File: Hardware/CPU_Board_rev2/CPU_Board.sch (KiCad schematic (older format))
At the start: 103 parts, among them P1 CONN_01X02, P10 CONN_01X02, P11 CONN_01X06, P12 CONN_01X03, P13 CONN_01X01, P14 CONN_01X03, P15 CONN_01X01, P16 CONN_01X01, P17 CONN_01X01, P18 CONN_01X03, P19 CONN_01X01, P2 USB_B, P20 CONN_01X01, P21 CONN_01X01, P22 CONN_01X01, P23 CONN_01X01, P24 CONN_01X01, P3 CONN_01X04, P4 CONN_01X04, P5 CONN_01X06, P6 CONN_01X02, P7 CONN_01X02, P8 CONN_01X02, P9 CONN_01X02, Q1 Q_PMOS_GSD, Q2 Q_PNP_BCE, Q3 Q_PNP_BCE, Q4 N-Channel, Q5 P-Channel, U1 STM32F411RETx, U10 MCDTS2-4N, U11 LPS22HB, U12 INA128, U2 NCP1117DT12G, U3 FT232RL, U4 HTS221, U5 INA128, U6 SPBTLE-RF, U7 A2235-H, U8 LSM303AGR, U9 LSM6DSL, Y1 8MHz

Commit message: PCB Rev 2 on the way
/Somewhat/ done with the layout
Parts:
- removed JP3: Jumper_NC_Small, Pin_Headers:Pin_Header_Straight_2x01_Pitch2.54mm, symbol Jumper_NC_Small
- removed P21, P24: CONN_01X01, Mounting_Holes:MountingHole_2.2mm_M2_DIN965_Pad, symbol CONN_01X01
- removed P6: CONN_01X02, Pin_Headers:Pin_Header_Straight_1x02_Pitch2.54mm, symbol CONN_01X02
- removed Q4: N-Channel, TO_SOT_Packages_SMD:SOT-23_Handsoldering, symbol N-Channel
- removed Q5: P-Channel, TO_SOT_Packages_SMD:SOT-23_Handsoldering, symbol P-Channel
- removed R10, R13: 5360, Resistors_SMD:R_0805_HandSoldering, symbol R
- removed R17, R19, R20: 1k, Resistors_SMD:R_0805_HandSoldering, symbol R
- added P21: CONN_01X06, Custom_Holes:Socket_Strip_Straight_1x06, symbol CONN_01X06
- added P24: CONN_01X06, Connectors_JST:JST_PH_S6B-PH-K_06x2.00mm_Angled, symbol CONN_01X06
- added P25, P26: CONN_01X04, Pin_Headers:Pin_Header_Straight_1x04_Pitch2.54mm, symbol CONN_01X04
- added R10, R13: 5k, Resistors_SMD:R_0805_HandSoldering, symbol R_Small
- added RV1, RV2: 360, Potentiometers:Potentiometer_Trimmer_Bourns_PV36W, symbol POT
- P19, P20, P22, P23: footprint Mounting_Holes:MountingHole_2.2mm_M2_DIN965_Pad -> FOOTPRINTS:MountingHole_2.2mm_M2_DIN965_NoPad
- P3, P4: footprint Pin_Headers:Pin_Header_Straight_1x04_Pitch2.54mm -> Connectors_JST:JST_PH_S4B-PH-K_04x2.00mm_Angled
- U2: footprint TO_SOT_Packages_SMD:TO-263-3Lead -> TO_SOT_Packages_SMD:SOT-223
- Y1: footprint Crystals:Crystal_SMD_EuroQuartz_MQ-4pin_7.0x5.0mm_HandSoldering -> Crystals:Crystal_SMD_HC49-SD
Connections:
- net +3V3: now also P21.6 (P6), P24.6 (P6)
- net +5V: now also C12.1, C16.1, C9.1, L2.2, Q3.2 (C), U2.3 (VI); no longer P1.2 (P2), Q1.3 (D)
- net +5VA: now also P3.4 (P4), P4.4 (P4), U12.7 (V+), U5.7 (V+), P25.4 (P4), P26.4 (P4)
- net BT_5_PA0: no longer P11.6 (P6), R9.2, U6.4 (SPI_IRQ)
- net BT_7_PB3: now also P11.2 (P2); no longer P11.3 (P3)
- net BT_8_PA6: now also P11.3 (P3); no longer P11.2 (P2)
- net GND: now also R16.1, P21.5 (P5), P24.5 (P5)
- net GNDA: now also P3.1 (P1), P4.1 (P1), U12.4 (V-), U12.5 (Ref), U5.4 (V-), U5.5 (Ref), P25.1 (P1), P26.1 (P1)
- net GPS_TOGGLE: now also R16.2, U7.19 (ON_OFF)
- net IMU_I2C_CL: now also P21.2 (P2), P24.2 (P2)
- net IMU_I2C_DA: now also P21.1 (P1), P24.1 (P1)
- net Load_cell_amp_1: now also U12.6; no longer U5.6
- net Load_cell_amp_2: now also U5.6; no longer U12.6
- net VL_C9: now reaches U1.40 (PC9/I2C3_SDA/I2S_CKIN/RCC_MCO_2/SDIO_D1/TIM3_CH4)
- net VL_C9: now also P21.3 (P3), P24.3 (P3)
- net VL_C10: now reaches U1.51 (PC10/I2S3_CK/SDIO_D2/SPI3_SCK)
- net VL_C10: now also P21.4 (P4), P24.4 (P4)
- net at U5.1 (Rg): now also R10.1, RV1.1, RV1.2
- net at P3.2 (P2), U5.2 (-): now also P25.2 (P2)
- net at P3.3 (P3), U5.3 (+): now also P25.3 (P3)
- net at U5.8 (Rg): now also R10.2, RV1.3
- net at U12.1 (Rg): now also R13.1, RV2.3
- net at P4.2 (P2), U12.2 (-): now also P26.2 (P2)
- net at P4.3 (P3), U12.3 (+): now also P26.3 (P3)
- net at U12.8 (Rg): now also R13.2, RV2.1, RV2.2
- new net: P1.2 (P2), Q1.3 (D)
- new net BT_4_PA0: P11.6 (P6), R9.2, U6.4 (SPI_IRQ)
- no-connect marks 58 -> 54
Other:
- note added: "Aimed for: 5.36 kohm"
- note added: "Amplifier for load cell,\nconnects to JST-TH and Analog"
- note added: "Shutdown"
- note added: "Time-of-Flight\nVL530x"
- note removed: "3V3/2 =\n1.65V"
- note removed: "Amplifier for load cell,\nconnects to TH and Analog"
- note removed: "High-speed digital \nswitching logic"
- note removed: "Pull to\nReference"
- moved on the sheet: C14, C18, L2, L3, R16

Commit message: Chackpoint PCB rev2
* Added datasheets for LSM9DS1 and STEVAL board
* Drawn footprints for:
o Connectors (JST)
o LGA-12_2x2mm "Handsolder friendlier"
o LGA-24L_3x3.5 "Handsolder friendlier"
* Drawn symbol for LSM9DS1
* Fixed GPS A2235-H footprints (normal & Handsolder)
* Almost completed MCU-board rev2 schematic (Miss connections for
LSM9DS1)
* Almost completed MCU-board rev2 PCB layout (Miss the connections for
LSM and have only designed internal module layout for all IMU/IMU-like
components.)

Next steps:
* Make space for gigantig STEVAL LSM9DS1 DIP24
* Draw connections to MCU
* Cake
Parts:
- removed C30: 4.7u, Capacitors_SMD:CP_Elec_4x5.3, symbol C
- added C30: 4.7u, Capacitors_SMD:CP_Elec_3x5.3, symbol CP
- added C34, C36, C37, C39: 100n, Capacitors_SMD:C_0805_HandSoldering, symbol C
- added C35: 10uF, Capacitors_SMD:CP_Elec_5x5.3, symbol CP1_Small
- added C38: 10n, Capacitors_SMD:C_0805_HandSoldering, symbol C
- added IM1: LSM9DS1, FOOTPRINTS:LGA-24L_3x3.5mm_Pitch0.43mm_Handsolder, symbol LSM9DS1
- added JP3, JP4: Jumper_NC_Dual, Pin_Headers:Pin_Header_Straight_1x03_Pitch2.54mm, symbol Jumper_NC_Dual
- added JP5: Jumper_NC_Small, Pin_Headers:Pin_Header_Straight_1x02_Pitch2.54mm, symbol Jumper_NC_Small
- added P6: CONN_02X12, Housings_DIP:DIP-24_W10.16mm, symbol CONN_02X12
- added R14: 220, Resistors_SMD:R_0805_HandSoldering, symbol R_Small
- added R17, R19: 10k, Resistors_SMD:R_0805_HandSoldering, symbol R
- C10, C4, C5: footprint Capacitors_SMD:CP_Elec_4x5.3 -> Capacitors_SMD:CP_Elec_3x5.3
- P24: footprint Connectors_JST:JST_PH_S6B-PH-K_06x2.00mm_Angled -> FOOTPRINTS:JST_PH_S6B-PH-K_06x2.50mm_Angled
- P3, P4: footprint Connectors_JST:JST_PH_S4B-PH-K_04x2.00mm_Angled -> FOOTPRINTS:Connector_JST_S4B-ZR_1x4
- U8: footprint Housings_LGA:LGA-12_2x2mm_Pitch0.5mm -> FOOTPRINTS:LGA-12_2x2mm_Pitch0.5mm_Handsolder
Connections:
- net +3V3: now also JP4.2, JP5.1, R17.1, R19.1; no longer D2.1 (K), U2.2 (VO), U2.4 (VO)
- net +5V: now also JP3.2, R14.1; no longer Q3.2 (C)
- net GND: now also C30.2, C34.2, C35.2, C36.2, C37.2, C38.2, C39.2, IM1.14 (RES), IM1.15 (RES), IM1.16 (RES), IM1.17 (RES), IM1.18 (RES), IM1.19 (GND), IM1.20 (GND), P6.13 (P13)
- net IMU_I2C_CL: now also IM1.2 (SCL/SPI), P6.20 (P20), R17.2
- net IMU_I2C_DA: now also R19.2
- net LPS_VDD: now also C30.1
- net USB3V3: now reaches U3.17 (3V3OUT)
- net USB3V3: now also C34.1, JP4.3
- net USB5V: now reaches C6.1, C7.1, C8.1, L1.2, U3.20 (VCC)
- net USB5V: now also JP3.3
- net BT_10_PA1 renamed BT_CL
- net BT_11_PA8 renamed BT_RST
- net BT_4_PA0 renamed BT_IRQ
- net BT_7_PB3 renamed BT_CS
- net BT_8_PA6 renamed BT_MISO
- net BT_9_PA7 renamed BT_MOSI
- new net: JP3.1, Q3.2 (C)
- new net: D2.1 (K), R14.2
- new net: JP4.1, U2.2 (VO), U2.4 (VO)
- new net: C38.1, IM1.21 (CAP)
- new net: C39.1, IM1.24 (C1)
- new net LSM9_CS_A/G: IM1.7 (CS_A/G), P6.19 (P19)
- new net LSM9_CS_M: IM1.8 (CS_M), P6.18 (P18)
- new net LSM9_DEN_A/G: IM1.13 (DEN_A/G), P6.23 (P23)
- new net LSM9_DRDY_M: IM1.9 (DRDY_M), P6.16 (P16)
- new net LSM9_INT1_A/G: IM1.11 (INT_A/G), P6.14 (P14)
- new net LSM9_INT2_A/G: IM1.12 (INT2_A/G), P6.15 (P15)
- new net LSM9_INT_M: IM1.10 (INT_M), P6.17 (P17)
- new net LSM9_SDA: IM1.4 (SDA/SDI/SDO), P6.21 (P21)
- new net LSM9_SDO: IM1.5 (SDO_A/G), IM1.6 (SDO_M), P6.22 (P22)
- new net LSM9_VDD: C35.1, C36.1, C37.1, IM1.1 (VDDIO), IM1.22 (VDD), IM1.23 (VDD), IM1.3 (VDDIO), JP5.2, P6.1 (P1), P6.2 (P2)
- no-connect marks 54 -> 64
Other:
- note added: "IMU Accelerometer/Gyroscope/Magnetometer\n("Backup")"
- moved on the sheet: C12, C14, C16, C18, C19, C20, C9, D2, L2, L3, U2

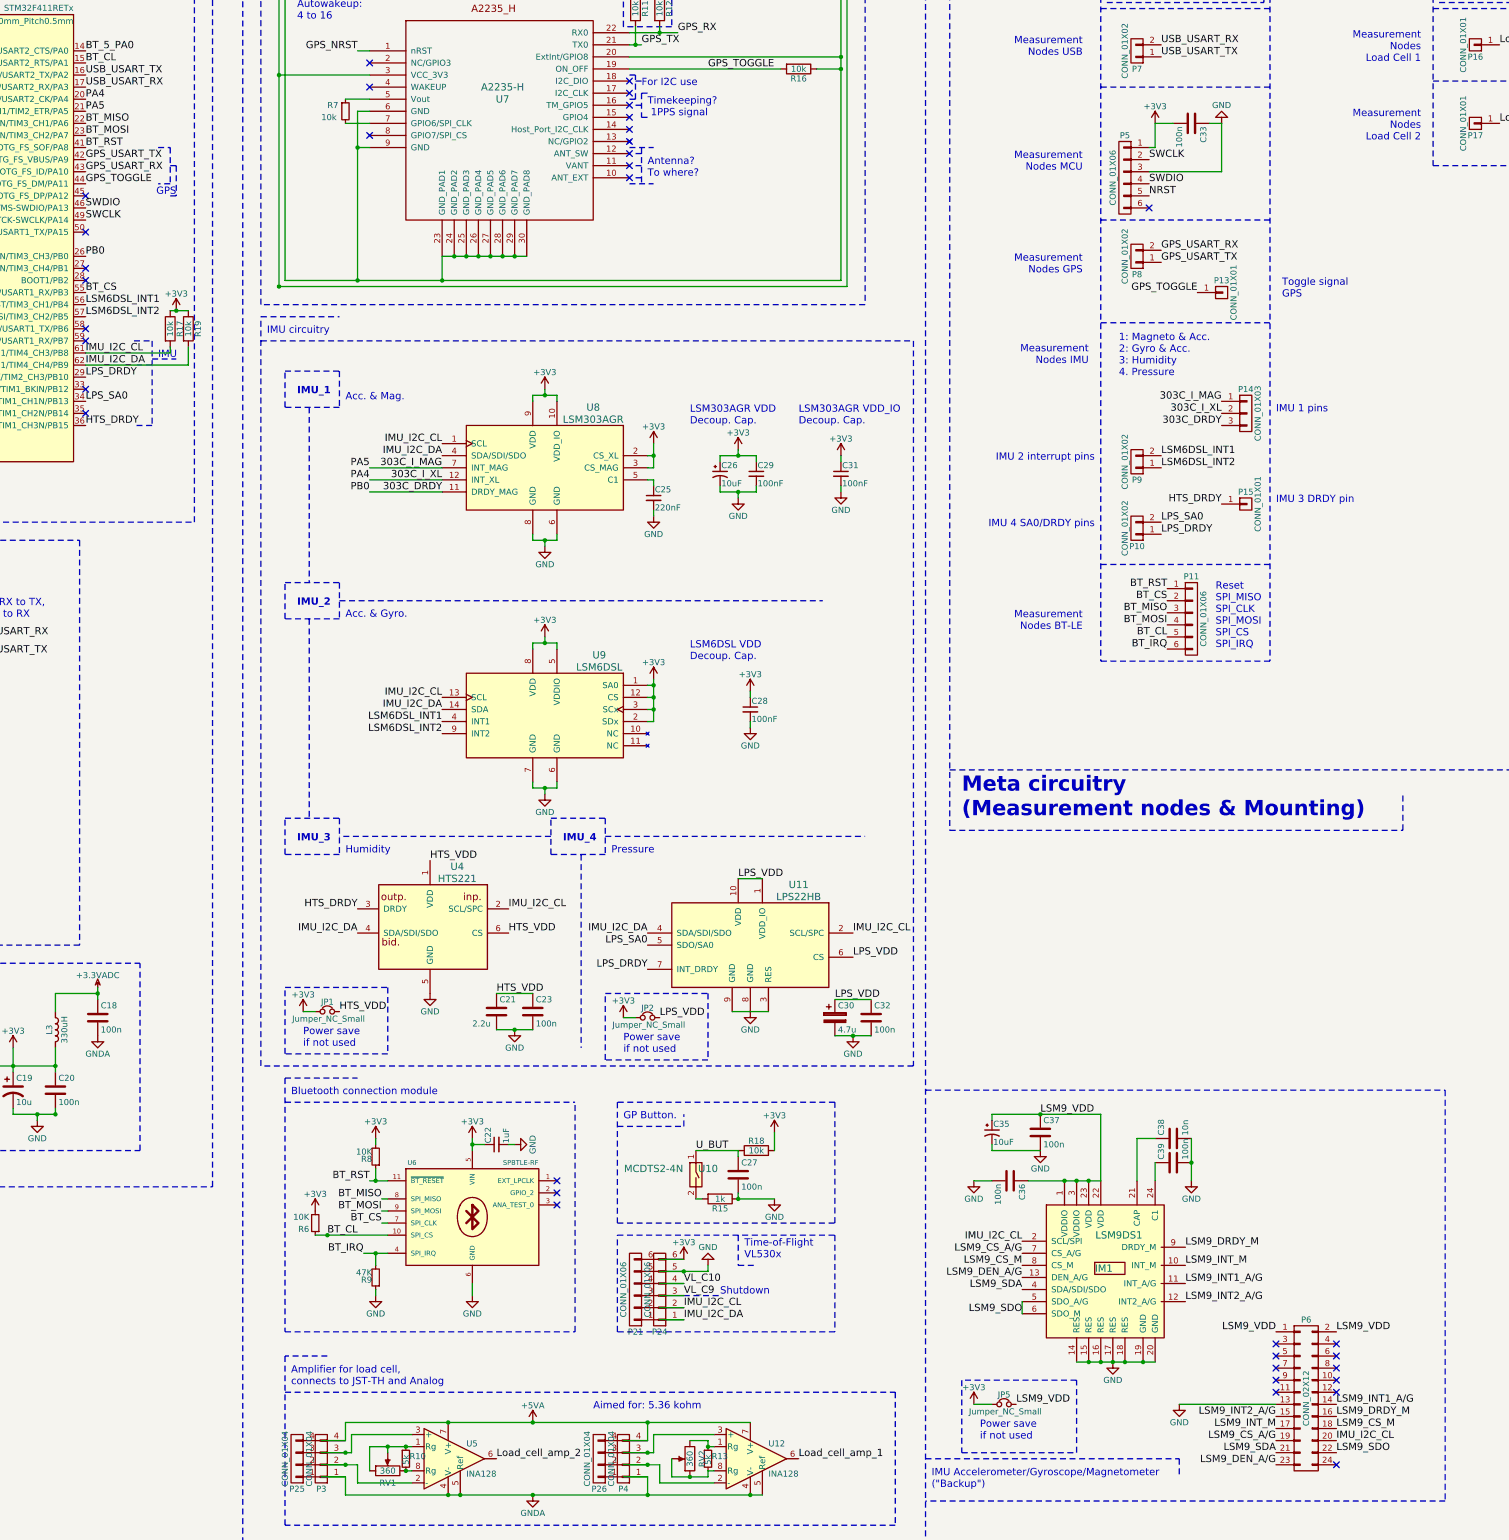
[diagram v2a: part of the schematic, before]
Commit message: PCB rev2.0 complete-ish
Rev 2 completed, except for LSM9DS1 ports: "SDO-A/G", "SDO-M" and "Data
enable A/G"
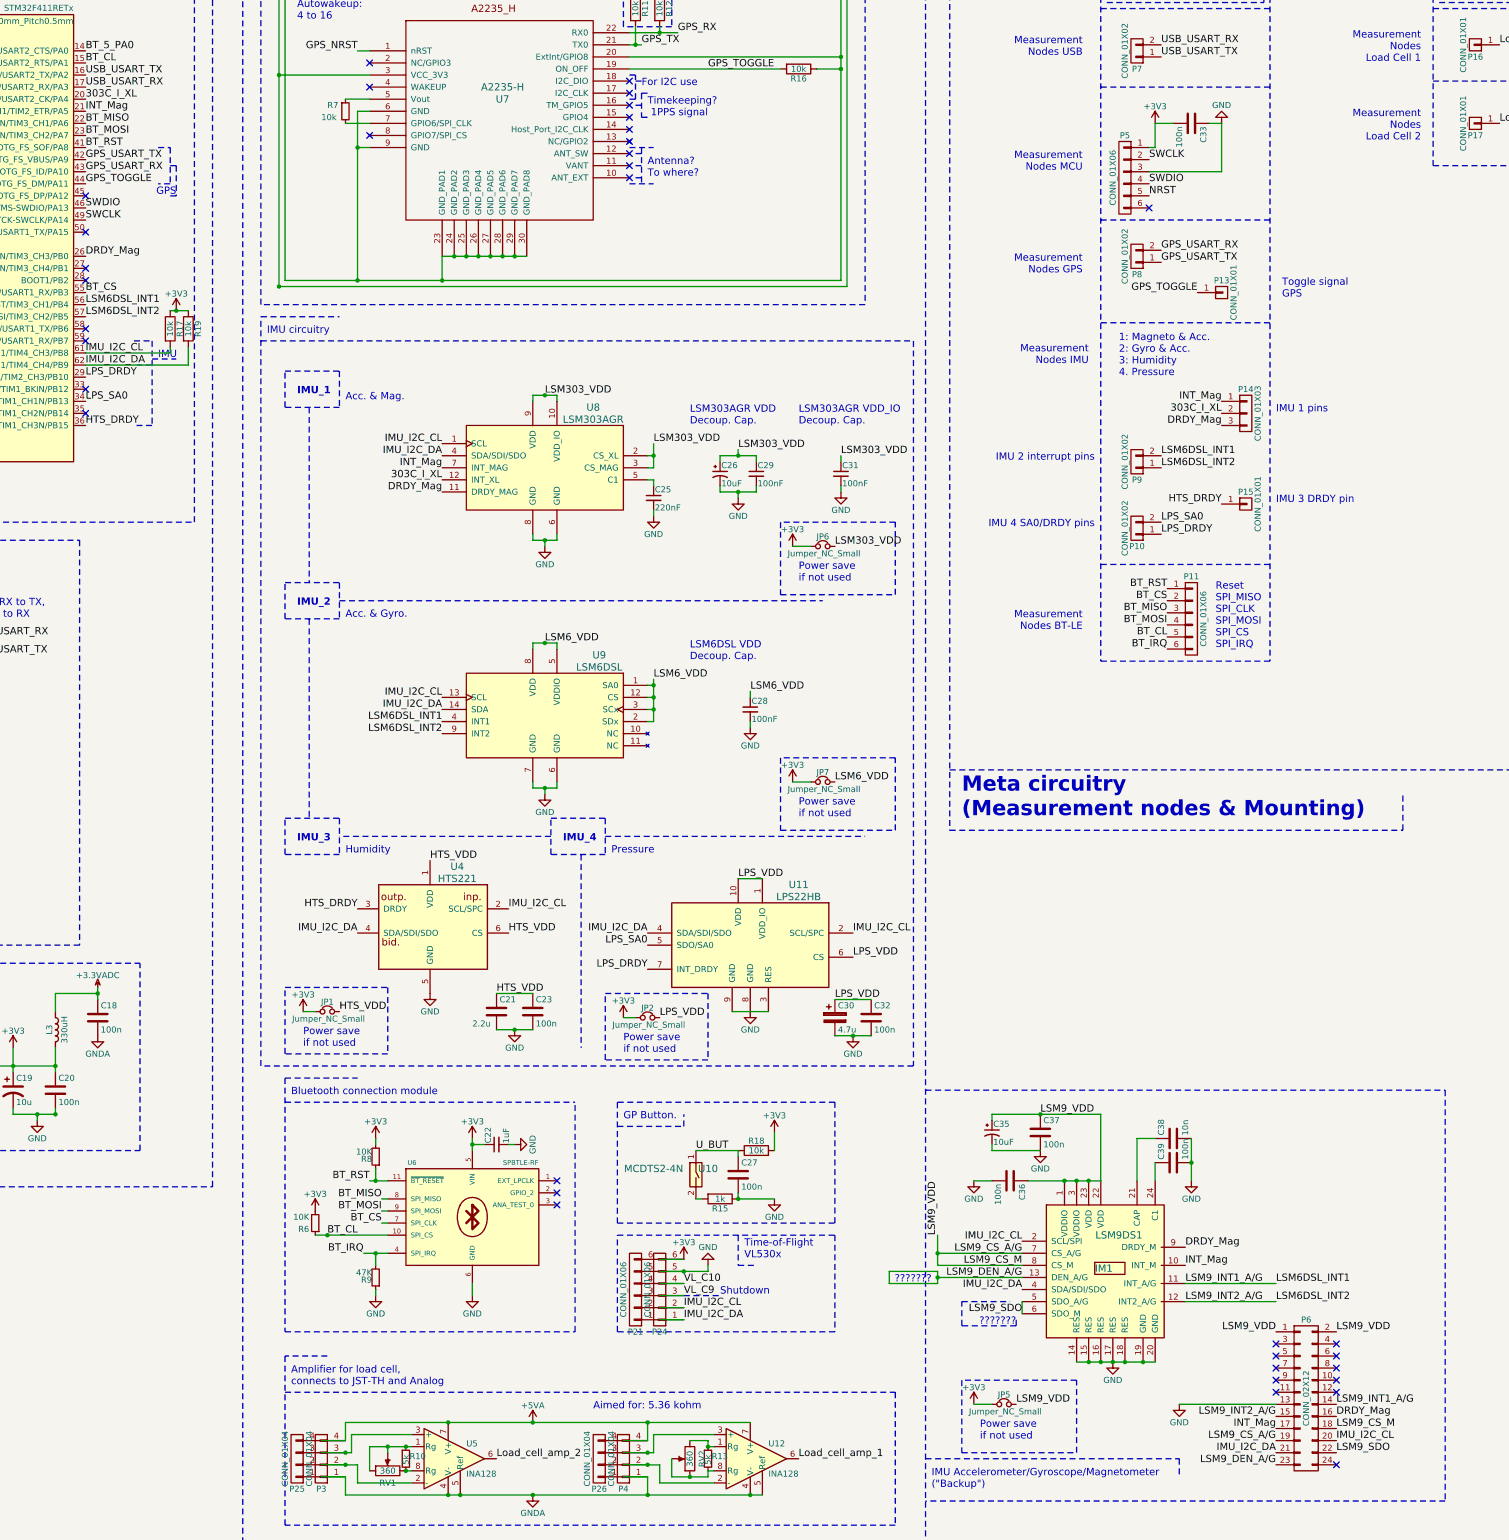
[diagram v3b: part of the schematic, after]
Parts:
- added JP6, JP7: Jumper_NC_Small, Pin_Headers:Pin_Header_Straight_1x02_Pitch2.54mm, symbol Jumper_NC_Small
- P6: footprint Housings_DIP:DIP-24_W10.16mm -> Housings_DIP:DIP-24_W15.24mm_Socket
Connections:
- net LSM9_CS_M is gone; now on net LSM9_CS_A/G: IM1.8 (CS_M), P6.18 (P18)
- net LSM9_DRDY_M is gone; now on net DRDY_Mag: IM1.9 (DRDY_M), P6.16 (P16)
- net LSM9_INT1_A/G is gone; now on net LSM6DSL_INT1: IM1.11 (INT_A/G), P6.14 (P14)
- net LSM9_INT2_A/G is gone; now on net LSM6DSL_INT2: IM1.12 (INT2_A/G), P6.15 (P15)
- net LSM9_INT_M is gone; now on net INT_Mag: IM1.10 (INT_M), P6.17 (P17)
- net LSM9_SDA is gone; now on net IMU_I2C_DA: IM1.4 (SDA/SDI/SDO), P6.21 (P21)
- net LSM9_VDD is gone; now on net LSM9_CS_A/G: C35.1, C36.1, C37.1, IM1.1 (VDDIO), IM1.22 (VDD), IM1.23 (VDD), IM1.3 (VDDIO), JP5.2, P6.1 (P1), P6.2 (P2)
- net +3V3: now also JP6.1, JP7.1; no longer C26.1, C28.1, C29.1, C31.1, U8.10 (VDD_IO), U8.2 (CS_XL), U8.3 (CS_MAG), U8.9 (VDD), U9.1 (SA0), U9.12 (CS), U9.2 (SDx), U9.3 (SCx), U9.5 (VDDIO), U9.8 (VDD)
- net 303C_DRDY renamed DRDY_Mag
- net 303C_I_MAG renamed INT_Mag
- new net LSM303_VDD: C26.1, C29.1, C31.1, JP6.2, U8.10 (VDD_IO), U8.2 (CS_XL), U8.3 (CS_MAG), U8.9 (VDD)
- new net LSM6_VDD: C28.1, JP7.2, U9.1 (SA0), U9.12 (CS), U9.2 (SDx), U9.3 (SCx), U9.5 (VDDIO), U9.8 (VDD)
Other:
- note added: "???????"

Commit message: PCB rev2 complete
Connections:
- net LSM9_SDO is gone; now on net GND: IM1.5 (SDO_A/G), IM1.6 (SDO_M), P6.22 (P22)
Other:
- note removed: "???????"
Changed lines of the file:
@@
 Text Label 17500 13100 0    60   ~ 0
 LSM6DSL_INT2
-Wire Wire Line
-	14700 12900 15400 12900
-Text Notes 14650 12950 2    60   ~ 0
-???????
-Wire Wire Line
-	14700 12850 14700 12950
-Wire Wire Line
-	14700 12850 14300 12850
-Wire Wire Line
-	14300 12850 14300 12950
-Wire Wire Line
-	14300 12950 14700 12950
-Connection ~ 14700 12900
 Text Label 15400 13000 2    60   ~ 0
 IMU_I2C_DA
 Text Label 17500 14350 2    60   ~ 0
 IMU_I2C_DA
-Text Notes 15350 13300 2    60   ~ 0
-???????
-Wire Notes Line
-	15350 13250 15350 13300
-Wire Notes Line
-	15350 13300 14900 13300
-Wire Notes Line
-	14900 13300 14900 13100
-Wire Notes Line
-	14900 13100 15300 13100
+$Comp
+L GND #PWR?
+U 1 1 5A01444D
+P 15400 13200
+F 0 "#PWR?" H 15400 12950 50  0001 C CNN
+F 1 "GND" H 15400 13050 50  0000 C CNN
+F 2 "" H 15400 13200 50  0001 C CNN
+F 3 "" H 15400 13200 50  0001 C CNN
+	1    15400 13200
+	1    0    0    -1
+$EndComp
 $EndSCHEMATC

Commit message: Fixes
Some fixes (now implemented to the PCB)
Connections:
- net BT_5_PA0 is gone; now on net BT_IRQ: U1.14 (ADC1_IN0/SYS_WKUP/TIM2_CH1/TIM2_ETR/TIM5_CH1/USART2_CTS/PA0)
- net BT_CL is gone; now on net BT_CS: P11.5 (P5), R6.1, U1.15 (ADC1_IN1/I2S4_SD/SPI4_MOSI/TIM2_CH2/TIM5_CH2/USART2_RTS/PA1), U6.10 (SPI_CS)
- net BT_CS: no longer P11.2 (P2), U1.55 (I2C2_SDA/I2S1_CK/I2S3_CK/SPI1_SCK/SPI3_SCK/SYS_JTDO-SWO/TIM2_CH2/USART1_RX/PB3), U6.7 (SPI_CLK)
- new net BT_CLK: P11.2 (P2), U1.55 (I2C2_SDA/I2S1_CK/I2S3_CK/SPI1_SCK/SPI3_SCK/SYS_JTDO-SWO/TIM2_CH2/USART1_RX/PB3), U6.7 (SPI_CLK)
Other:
- note added: "Reset\nSPI_CLK\nSPI_MISO\nSPI_MOSI\nSPI_CS\nSPI_IRQ"
- note removed: "Reset\nSPI_MISO\nSPI_CLK\nSPI_MOSI\nSPI_CS\nSPI_IRQ"
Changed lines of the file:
@@
 BT_MOSI
 Text Label 10100 12450 2    60   ~ 0
+BT_CLK
+Text Label 9650 12550 0    60   ~ 0
 BT_CS
-Text Label 9650 12550 0    60   ~ 0
-BT_CL
 $Comp
 L R_Small R9
@@
 BT_MOSI
 Text Label 16600 7300 2    60   ~ 0
+BT_CLK
+Text Label 16600 7600 2    60   ~ 0
 BT_CS
-Text Label 16600 7600 2    60   ~ 0
-BT_CL
 Text Label 16600 7700 2    60   ~ 0
 BT_IRQ
-Text Notes 17000 7700 0    60   ~ 0
-Reset\nSPI_MISO\nSPI_CLK\nSPI_MOSI\nSPI_CS\nSPI_IRQ
+Text Notes 16950 7700 0    60   ~ 0
+Reset\nSPI_CLK\nSPI_MISO\nSPI_MOSI\nSPI_CS\nSPI_IRQ
 $Comp
 L CONN_01X06 P11
@@
 BT_MOSI
 Text Label 7650 4750 0    60   ~ 0
+BT_CLK
+Text Label 7650 2850 0    60   ~ 0
 BT_CS
-Text Label 7650 2850 0    60   ~ 0
-BT_CL
 Text Label 7650 2750 0    60   ~ 0
-BT_5_PA0
+BT_IRQ
 $Comp
 L STM32F411RETx U1
@@
 Wire Wire Line
 	12200 2000 12200 2250
-Connection ~ 9250 4700
 Wire Wire Line
 	9250 2000 9250 4700
@@
 IMU_I2C_DA
 $Comp
-L GND #PWR?
+L GND #PWR078
 U 1 1 5A01444D
 P 15400 13200
-F 0 "#PWR?" H 15400 12950 50  0001 C CNN
+F 0 "#PWR078" H 15400 12950 50  0001 C CNN
 F 1 "GND" H 15400 13050 50  0000 C CNN
 F 2 "" H 15400 13200 50  0001 C CNN

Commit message: Rev 2 last ed. Rev 3 "merge"
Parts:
- C25: value 220nF -> 100nF
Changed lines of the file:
@@
 P 12350 6450
 F 0 "C25" H 12360 6520 50  0000 L CNN
-F 1 "220nF" H 12360 6370 50  0000 L CNN
+F 1 "100nF" H 12360 6370 50  0000 L CNN
 F 2 "Capacitors_SMD:C_0805_HandSoldering" H 12350 6450 50  0001 C CNN
 F 3 "" H 12350 6450 50  0001 C CNN
